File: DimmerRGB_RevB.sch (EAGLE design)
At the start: 61 parts, among them CON1 CON_10X200MIL, CON2 CON_5X100MIL, IC1 PIC16F18325, IC2 LM2931_ADJ, IC3 LM5111, IC4 LM5111, IC5 74HC14D, Q2 N-PWR-MOSFETLFPAK, Q3 N-PWR-MOSFETLFPAK, Q4 N-PWR-MOSFETLFPAK, Q5 N-PWR-MOSFETLFPAK, SW1 PEC11R, SW2 PEC11R, SW3 PEC09, SW4 PEC09

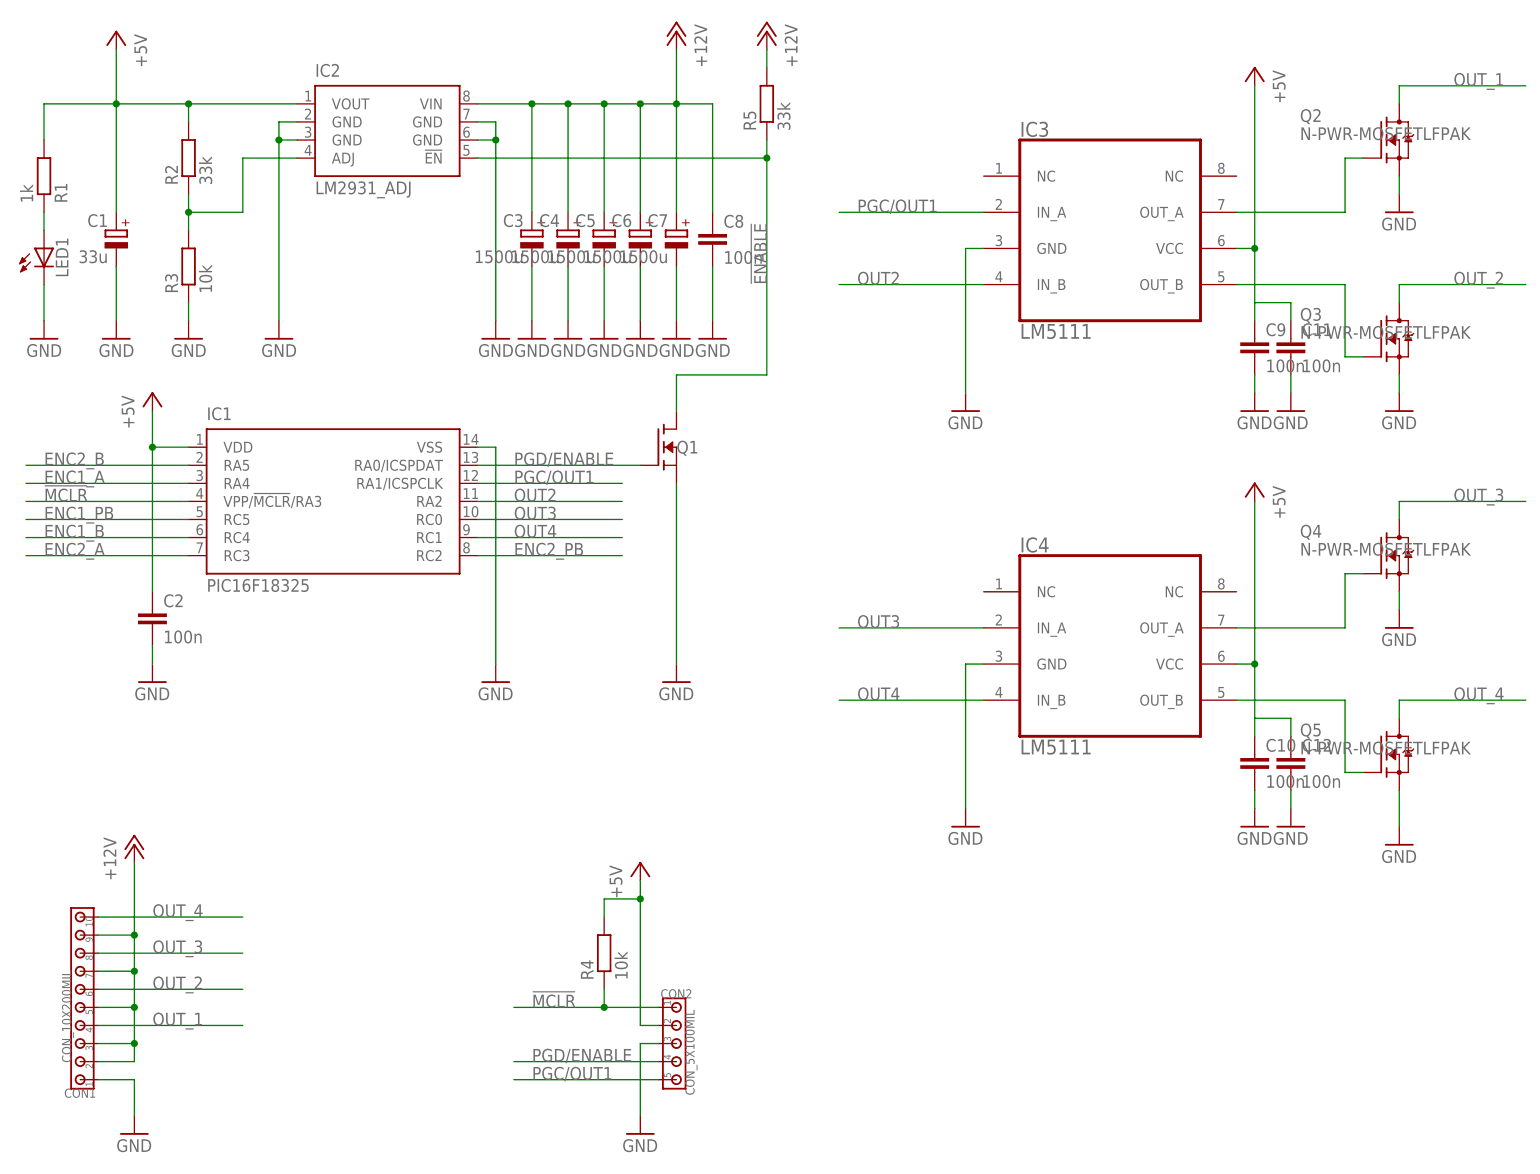
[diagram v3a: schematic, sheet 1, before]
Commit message: Linear regulator changed
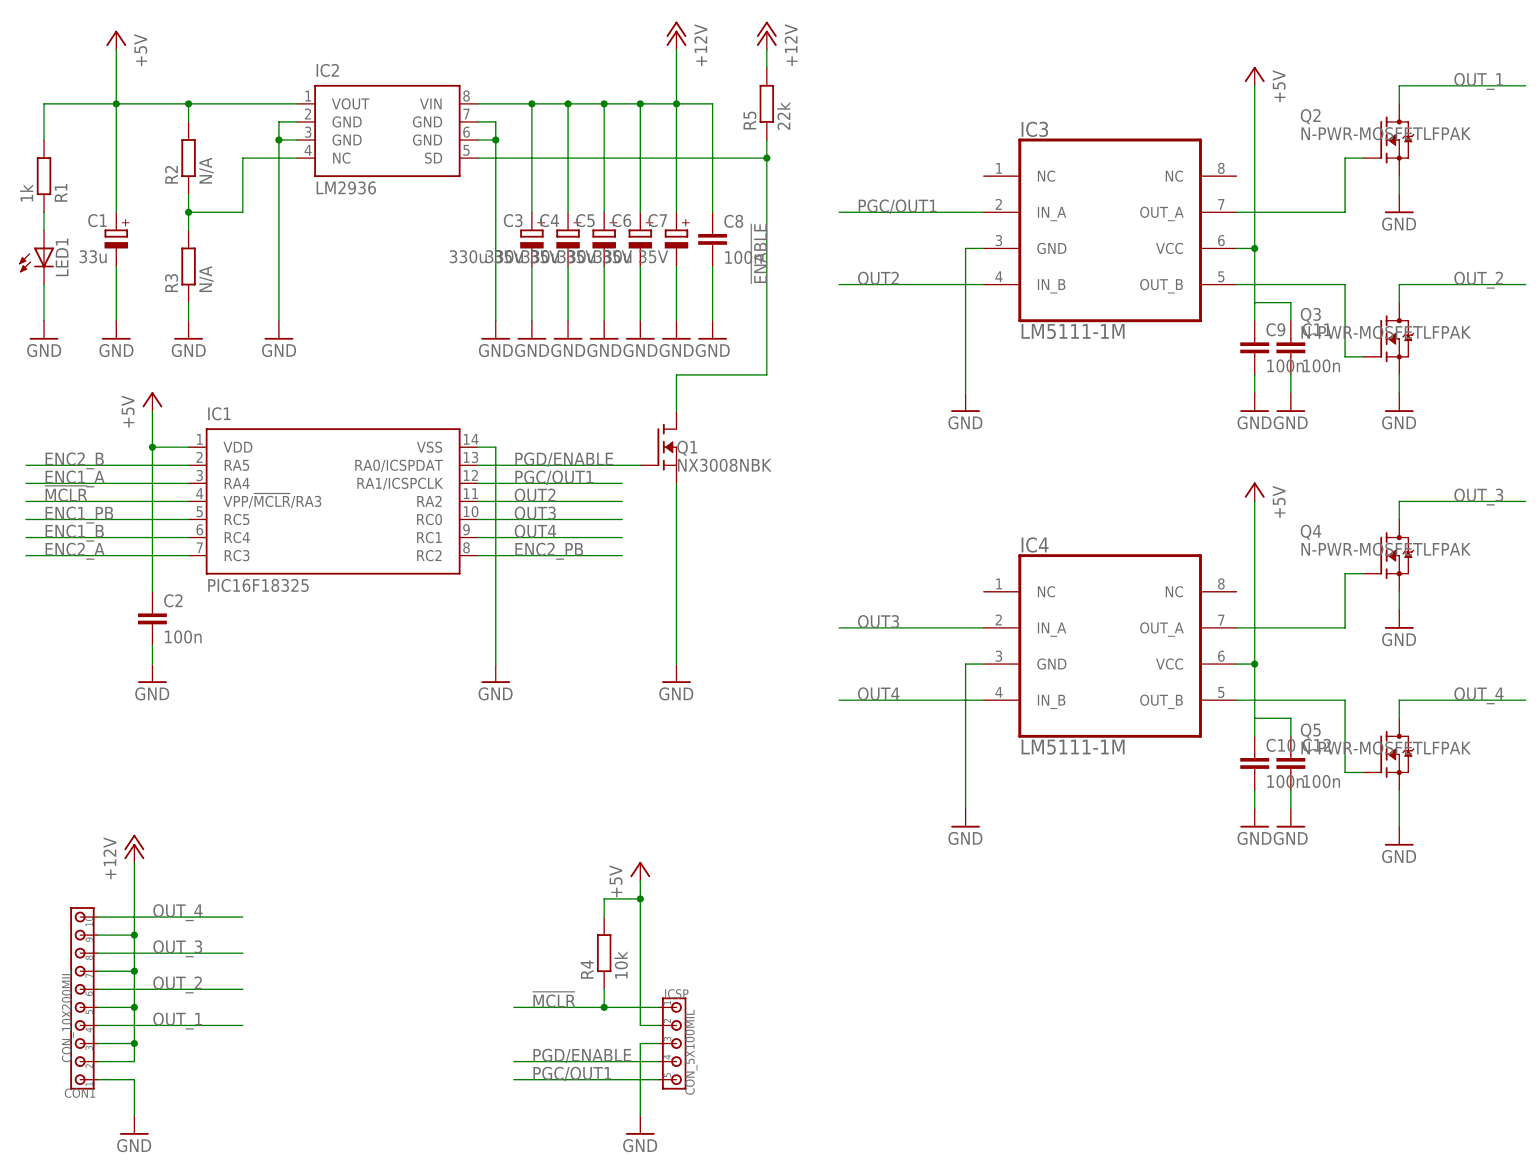
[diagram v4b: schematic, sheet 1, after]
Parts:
- C3, C4, C5, C6, C7: value 1500u -> 330u 35V
- IC2: value LM2931_ADJ -> LM2936; device 00VoltageRegulator:LM2931_ADJ -> 00VoltageRegulator:LM2936
- IC3, IC4: value LM5111 -> LM5111-1M
- Q1: value (none) -> NX3008NBK
- R2: value 33k -> N/A
- R3: value 10k -> N/A
- R5: value 33k -> 22k
- renumbered CON2 to ICSP
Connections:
- net !ENABLE!: now also IC2.SD; no longer IC2.!EN!
- net N$8: now also IC2.NC; no longer IC2.ADJ
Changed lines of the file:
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@@
 <part name="Q5" library="00Mosfet" deviceset="N-PWR-MOSFET" device="LFPAK" value="N-PWR-MOSFETLFPAK"/>
 <part name="Q4" library="00Mosfet" deviceset="N-PWR-MOSFET" device="LFPAK" value="N-PWR-MOSFETLFPAK"/>
-<part name="IC4" library="00Logic" deviceset="LM5111" device=""/>
-<part name="IC2" library="00VoltageRegulator" deviceset="LM2931_ADJ" device=""/>
+<part name="IC4" library="00Logic" deviceset="LM5111" device="" value="LM5111-1M"/>
+<part name="IC2" library="00VoltageRegulator" deviceset="LM2936" device=""/>
 <part name="C1" library="00Capacitor" deviceset="C_POLARIZED" device="SMC_C" value="33u"/>
 <part name="C10" library="00Capacitor" deviceset="C" device="C0805" value="100n"/>
@@
 <part name="GND20" library="00Supply" deviceset="GND" device=""/>
 <part name="Q3" library="00Mosfet" deviceset="N-PWR-MOSFET" device="LFPAK" value="N-PWR-MOSFETLFPAK"/>
-<part name="IC3" library="00Logic" deviceset="LM5111" device=""/>
+<part name="IC3" library="00Logic" deviceset="LM5111" device="" value="LM5111-1M"/>
 <part name="C9" library="00Capacitor" deviceset="C" device="C0805" value="100n"/>
 <part name="GND24" library="00Supply" deviceset="GND" device=""/>
@@
 <part name="GND29" library="00Supply" deviceset="GND" device=""/>
 <part name="CON1" library="00Connector" deviceset="CON_10X" device="200MIL"/>
-<part name="C7" library="00Capacitor" deviceset="C_POLARIZED" device="10MM" value="1500u"/>
-<part name="C5" library="00Capacitor" deviceset="C_POLARIZED" device="10MM" value="1500u"/>
-<part name="C4" library="00Capacitor" deviceset="C_POLARIZED" device="10MM" value="1500u"/>
-<part name="C3" library="00Capacitor" deviceset="C_POLARIZED" device="10MM" value="1500u"/>
+<part name="C7" library="00Capacitor" deviceset="C_POLARIZED" device="10MM" value="330u 35V"/>
+<part name="C5" library="00Capacitor" deviceset="C_POLARIZED" device="10MM" value="330u 35V"/>
+<part name="C4" library="00Capacitor" deviceset="C_POLARIZED" device="10MM" value="330u 35V"/>
+<part name="C3" library="00Capacitor" deviceset="C_POLARIZED" device="10MM" value="330u 35V"/>
 <part name="IC1" library="00PIC" deviceset="PIC16F18325" device=""/>
 <part name="FRAME2" library="frames" deviceset="A4L-LOC" device=""/>
@@
 <part name="R1" library="00Resistor" deviceset="RESISTOR" device="R0805" value="1k"/>
 <part name="GND1" library="00Supply" deviceset="GND" device=""/>
-<part name="Q1" library="00Mosfet" deviceset="N-FET" device="SOT23"/>
+<part name="Q1" library="00Mosfet" deviceset="N-FET" device="SOT23" value="NX3008NBK"/>
 <part name="GND15" library="00Supply" deviceset="GND" device=""/>
 <part name="GND6" library="00Supply" deviceset="GND" device=""/>
-<part name="R5" library="00Resistor" deviceset="RESISTOR" device="R0805" value="33k"/>
+<part name="R5" library="00Resistor" deviceset="RESISTOR" device="R0805" value="22k"/>
 <part name="P+6" library="00Supply" deviceset="+12V" device=""/>
-<part name="R2" library="00Resistor" deviceset="RESISTOR" device="R0805" value="33k"/>
-<part name="R3" library="00Resistor" deviceset="RESISTOR" device="R0805" value="10k"/>
+<part name="R2" library="00Resistor" deviceset="RESISTOR" device="R0805" value="N/A"/>
+<part name="R3" library="00Resistor" deviceset="RESISTOR" device="R0805" value="N/A"/>
 <part name="GND5" library="00Supply" deviceset="GND" device=""/>
-<part name="C6" library="00Capacitor" deviceset="C_POLARIZED" device="10MM" value="1500u"/>
+<part name="C6" library="00Capacitor" deviceset="C_POLARIZED" device="10MM" value="330u 35V"/>
 <part name="GND12" library="00Supply" deviceset="GND" device=""/>
 <part name="P+7" library="00Supply" deviceset="+5V" device=""/>
@@
 <part name="GND38" library="00Supply" deviceset="GND" device=""/>
 <part name="GND32" library="00Supply" deviceset="GND" device=""/>
-<part name="CON2" library="00Connector" deviceset="CON_5X" device="100MIL"/>
+<part name="ICSP" library="00Connector" deviceset="CON_5X" device="100MIL"/>
 <part name="C8" library="00Capacitor" deviceset="C" device="C0805" value="100n"/>
 <part name="GND16" library="00Supply" deviceset="GND" device=""/>
@@
 <instance part="P+7" gate="1" x="200.66" y="162.56" rot="MR0"/>
 <instance part="P+8" gate="1" x="200.66" y="104.14" rot="MR0"/>
-<instance part="CON2" gate="G$1" x="119.38" y="30.48" rot="R270"/>
+<instance part="ICSP" gate="G$1" x="119.38" y="30.48" rot="R270"/>
 <instance part="C8" gate="G$1" x="124.46" y="139.7"/>
 <instance part="GND16" gate="1" x="124.46" y="124.46" rot="MR0"/>
@@
 <wire x1="114.3" y1="25.4" x2="114.3" y2="15.24" width="0.1524" layer="91"/>
 <pinref part="GND13" gate="1" pin="GND"/>
-<pinref part="CON2" gate="G$1" pin="3"/>
+<pinref part="ICSP" gate="G$1" pin="3"/>
 </segment>
 <segment>
@@
 <junction x="114.3" y="45.72"/>
 <pinref part="P+4" gate="1" pin="+5V"/>
-<pinref part="CON2" gate="G$1" pin="2"/>
+<pinref part="ICSP" gate="G$1" pin="2"/>
 </segment>
 <segment>
@@
 <junction x="109.22" y="30.48"/>
 <label x="99.06" y="30.48" size="1.778" layer="95"/>
-<pinref part="CON2" gate="G$1" pin="1"/>
+<pinref part="ICSP" gate="G$1" pin="1"/>
 </segment>
 <segment>
@@
 <wire x1="116.84" y1="20.32" x2="96.52" y2="20.32" width="0.1524" layer="91"/>
 <label x="99.06" y="20.32" size="1.778" layer="95"/>
-<pinref part="CON2" gate="G$1" pin="5"/>
+<pinref part="ICSP" gate="G$1" pin="5"/>
 </segment>
 </net>
@@
 <wire x1="116.84" y1="22.86" x2="96.52" y2="22.86" width="0.1524" layer="91"/>
 <label x="99.06" y="22.86" size="1.778" layer="95"/>
-<pinref part="CON2" gate="G$1" pin="4"/>
+<pinref part="ICSP" gate="G$1" pin="4"/>
 </segment>
 </net>
@@
 <net name="!ENABLE!" class="0">
 <segment>
-<pinref part="IC2" gate="G$1" pin="!EN!"/>
+<pinref part="IC2" gate="G$1" pin="SD"/>
 <wire x1="91.44" y1="149.86" x2="132.08" y2="149.86" width="0.1524" layer="91"/>
 <pinref part="R5" gate="G$1" pin="1"/>
@@
 <pinref part="R3" gate="G$1" pin="2"/>
 <wire x1="50.8" y1="144.78" x2="50.8" y2="142.24" width="0.1524" layer="91"/>
-<pinref part="IC2" gate="G$1" pin="ADJ"/>
+<pinref part="IC2" gate="G$1" pin="NC"/>
 <wire x1="50.8" y1="142.24" x2="50.8" y2="139.7" width="0.1524" layer="91"/>
 <wire x1="66.04" y1="149.86" x2="58.42" y2="149.86" width="0.1524" layer="91"/>
